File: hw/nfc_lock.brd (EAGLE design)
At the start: 100 x 80 mm, 10 parts, among them IC1 STM8S003F3, IC3 MCP170312MB, U1 M24SR16-YMN6T/2, X1 MINI-USB-32005-301

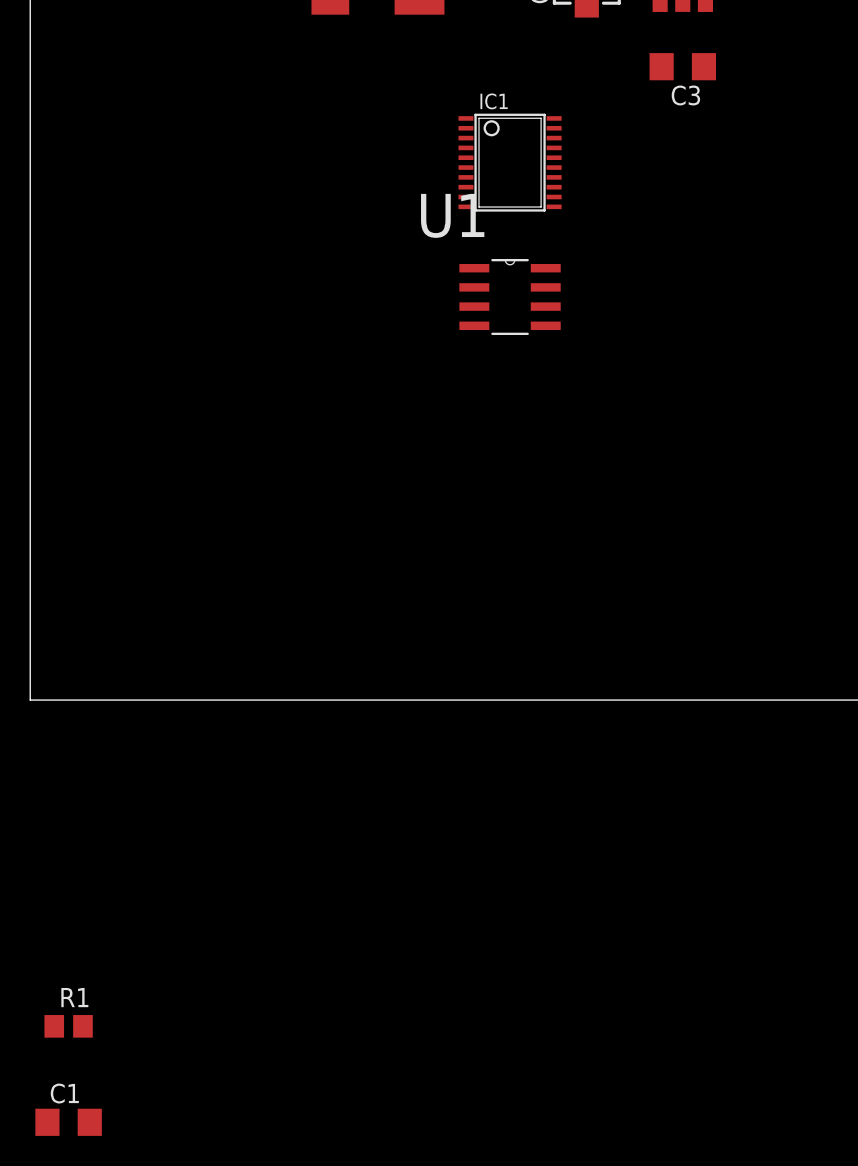
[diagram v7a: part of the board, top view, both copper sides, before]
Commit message: 2x n-mosfet for PWM of servos
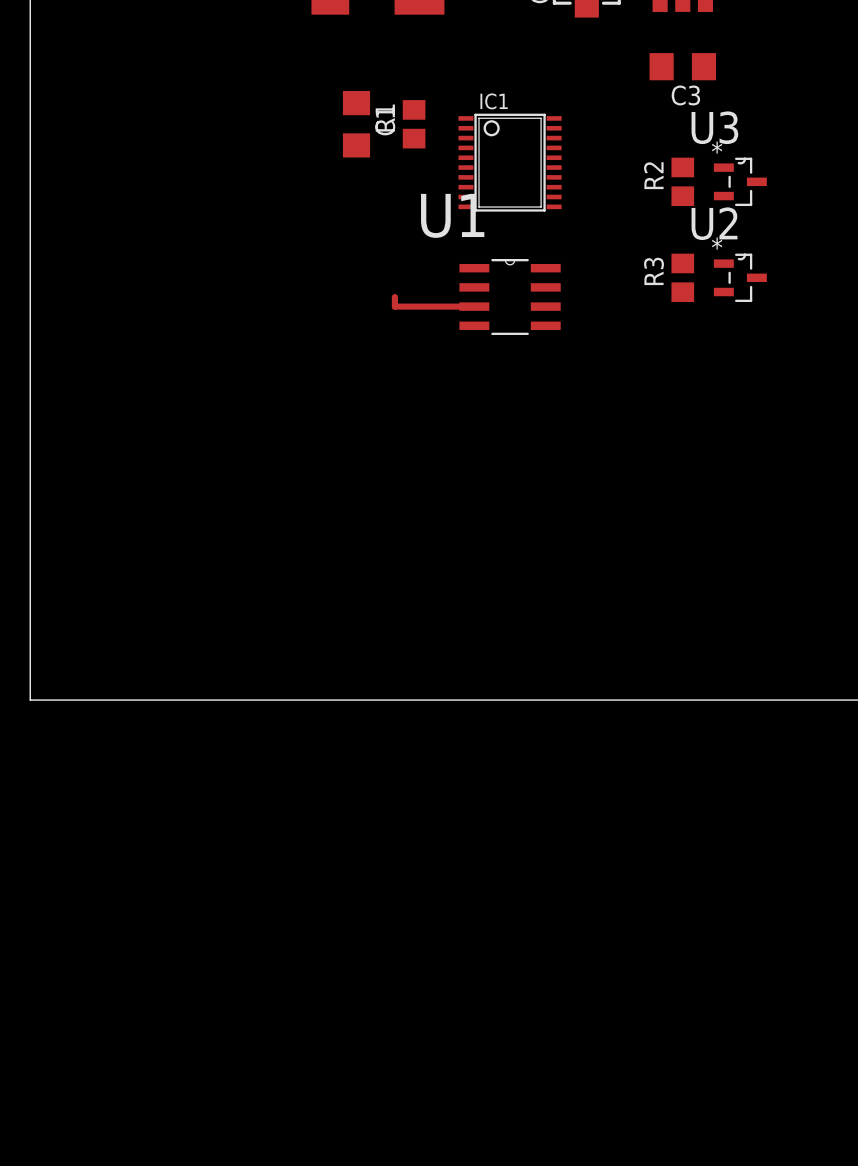
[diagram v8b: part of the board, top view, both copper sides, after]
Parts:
- added R2, R3: 10k, rcl:R0805
- added U2, U3: IRFML8244TRPBF, irfml8244trpbf:SOT95P240X112-3N
- moved C1 68.7 mm to (21.6, 38.1), turned to 270 degrees
- moved R1 63.9 mm to (25.4, 38.1), turned to 90 degrees
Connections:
- net N$3 renamed +5V/2
- new net N$10: U1.2, U1.3
- new net N$13: IC1.15, R2.2, U3.1
- new net N$3: IC1.14, R3.2, U2.1
- net 0V: now also R2.1, R3.1, U2.2, U3.2
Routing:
- net N$10: track 0.00 -> 5.89 mm
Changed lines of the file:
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@@
 <attribute name="OC_NEWARK" value="unknown" x="22.86" y="50.8" size="1.778" layer="27" display="off"/>
 </element>
-<element name="R1" library="rcl" package="R0805" value="10k" x="2.54" y="-21.59"/>
-<element name="C1" library="rcl" package="C1206" value="10nF" x="2.54" y="-27.94"/>
+<element name="R1" library="rcl" package="R0805" value="10k" x="25.4" y="38.1" rot="R90"/>
+<element name="C1" library="rcl" package="C1206" value="10nF" x="21.59" y="38.1" rot="R270"/>
+<element name="U3" library="irfml8244trpbf" package="SOT95P240X112-3N" value="IRFML8244TRPBF" x="46.99" y="34.29">
+<attribute name="PACKAGE" value="SOT-23-3" x="46.99" y="34.29" size="1.778" layer="27" display="off"/>
+<attribute name="SUPPLIER" value="INTERNATIONAL RECTIFIER" x="46.99" y="34.29" size="1.778" layer="27" display="off"/>
+<attribute name="OC_FARNELL" value="1857298" x="46.99" y="34.29" size="1.778" layer="27" display="off"/>
+<attribute name="MPN" value="IRFML8244TRPBF" x="46.99" y="34.29" size="1.778" layer="27" display="off"/>
+<attribute name="OC_NEWARK" value="25T5496" x="46.99" y="34.29" size="1.778" layer="27" display="off"/>
+</element>
+<element name="R2" library="rcl" package="R0805" value="10k" x="43.18" y="34.29" rot="R90"/>
+<element name="U2" library="irfml8244trpbf" package="SOT95P240X112-3N" value="IRFML8244TRPBF" x="46.99" y="27.94">
+<attribute name="PACKAGE" value="SOT-23-3" x="46.99" y="27.94" size="1.778" layer="27" display="off"/>
+<attribute name="SUPPLIER" value="INTERNATIONAL RECTIFIER" x="46.99" y="27.94" size="1.778" layer="27" display="off"/>
+<attribute name="OC_FARNELL" value="1857298" x="46.99" y="27.94" size="1.778" layer="27" display="off"/>
+<attribute name="MPN" value="IRFML8244TRPBF" x="46.99" y="27.94" size="1.778" layer="27" display="off"/>
+<attribute name="OC_NEWARK" value="25T5496" x="46.99" y="27.94" size="1.778" layer="27" display="off"/>
+</element>
+<element name="R3" library="rcl" package="R0805" value="10k" x="43.18" y="27.94" rot="R90"/>
 </elements>
 <signals>
@@
 <contactref element="U1" pad="4"/>
 <contactref element="C1" pad="2"/>
+<contactref element="U3" pad="2"/>
+<contactref element="R2" pad="1"/>
+<contactref element="U2" pad="2"/>
+<contactref element="R3" pad="1"/>
 <wire x1="41.78" y1="41.91" x2="41.681" y2="46.279" width="0" layer="19" extent="1-1"/>
 <wire x1="36.83" y1="46.46" x2="41.681" y2="46.279" width="0" layer="19" extent="1-1"/>
+<wire x1="43.18" y1="33.34" x2="41.78" y2="41.91" width="0" layer="19" extent="1-1"/>
+<wire x1="45.8978" y1="33.3502" x2="43.18" y2="33.34" width="0" layer="19" extent="1-1"/>
+<wire x1="45.8978" y1="27.0002" x2="45.8978" y2="33.3502" width="0" layer="19" extent="1-1"/>
+<wire x1="43.18" y1="26.99" x2="45.8978" y2="27.0002" width="0" layer="19" extent="1-1"/>
 <wire x1="25.86" y1="49.2" x2="36.83" y2="46.46" width="0" layer="19" extent="1-1"/>
-<wire x1="28.8322" y1="34.585" x2="36.83" y2="46.46" width="0" layer="19" extent="1-1"/>
+<wire x1="21.59" y1="36.7" x2="25.86" y2="49.2" width="0" layer="19" extent="1-1"/>
+<wire x1="28.8322" y1="34.585" x2="21.59" y2="36.7" width="0" layer="19" extent="1-1"/>
 <wire x1="29.3878" y1="24.765" x2="28.8322" y2="34.585" width="0" layer="19" extent="1-1"/>
-<wire x1="3.94" y1="-27.94" x2="29.3878" y2="24.765" width="0" layer="19" extent="1-1"/>
 </signal>
 <signal name="+5V/1">
@@
 <wire x1="34.1122" y1="28.575" x2="44.58" y2="41.91" width="0" layer="19" extent="1-1"/>
 <wire x1="28.8322" y1="33.285" x2="34.1122" y2="28.575" width="0" layer="19" extent="1-1"/>
-<wire x1="1.59" y1="-21.59" x2="34.1122" y2="28.575" width="0" layer="19" extent="1-1"/>
+<wire x1="25.4" y1="37.15" x2="28.8322" y2="33.285" width="0" layer="19" extent="1-1"/>
 </signal>
 <signal name="+5V">
@@
 <wire x1="25.86" y1="52.4" x2="31.75" y2="50.02" width="0" layer="19" extent="1-1"/>
 </signal>
-<signal name="N$3">
-<contactref element="D1" pad="K"/>
-<contactref element="D2" pad="A"/>
-<wire x1="39.86" y1="54.61" x2="31.75" y2="54.12" width="0" layer="19" extent="1-1"/>
-</signal>
 <signal name="N$4">
 <contactref element="IC3" pad="2@1"/>
 <contactref element="D2" pad="K"/>
 <contactref element="C2" pad="+"/>
+<wire x1="43.18" y1="49.2" x2="43.96" y2="54.61" width="0" layer="19" extent="1-1"/>
 <wire x1="36.83" y1="50.06" x2="43.18" y2="49.2" width="0" layer="19" extent="1-1"/>
-<wire x1="43.96" y1="54.61" x2="43.18" y2="49.2" width="0" layer="19" extent="1-1"/>
 </signal>
 <signal name="N$5">
@@
 <contactref element="R1" pad="2"/>
 <contactref element="IC1" pad="4"/>
-<wire x1="3.49" y1="-21.59" x2="28.8322" y2="36.535" width="0" layer="19" extent="1-1"/>
-<wire x1="1.14" y1="-27.94" x2="3.49" y2="-21.59" width="0" layer="19" extent="1-1"/>
+<wire x1="21.59" y1="39.5" x2="25.4" y2="39.05" width="0" layer="19" extent="1-1"/>
+<wire x1="28.8322" y1="36.535" x2="25.4" y2="39.05" width="0" layer="19" extent="1-1"/>
 </signal>
 <signal name="N$6">
@@
 <wire x1="34.1122" y1="27.305" x2="34.6678" y2="33.935" width="0" layer="19" extent="1-1"/>
 </signal>
+<signal name="+5V/2">
+<contactref element="D1" pad="K"/>
+<contactref element="D2" pad="A"/>
+<wire x1="31.75" y1="54.12" x2="39.86" y2="54.61" width="0" layer="19" extent="1-1"/>
+</signal>
+<signal name="N$3">
+<contactref element="IC1" pad="14"/>
+<contactref element="U2" pad="1"/>
+<contactref element="R3" pad="2"/>
+<wire x1="43.18" y1="28.89" x2="45.8978" y2="28.8798" width="0" layer="19" extent="1-1"/>
+<wire x1="34.6678" y1="34.585" x2="43.18" y2="28.89" width="0" layer="19" extent="1-1"/>
+</signal>
+<signal name="N$10">
+<contactref element="U1" pad="3"/>
+<contactref element="U1" pad="2"/>
+<wire x1="29.3878" y1="26.035" x2="24.13" y2="26.035" width="0.4064" layer="1"/>
+<wire x1="24.13" y1="26.035" x2="24.13" y2="26.67" width="0.4064" layer="1"/>
+<wire x1="29.3878" y1="26.035" x2="29.3878" y2="27.305" width="0" layer="19" extent="1-1"/>
+</signal>
+<signal name="N$13">
+<contactref element="U3" pad="1"/>
+<contactref element="R2" pad="2"/>
+<contactref element="IC1" pad="15"/>
+<wire x1="43.18" y1="35.24" x2="45.8978" y2="35.2298" width="0" layer="19" extent="1-1"/>
+<wire x1="34.6678" y1="35.235" x2="43.18" y2="35.24" width="0" layer="19" extent="1-1"/>
+</signal>
 </signals>
